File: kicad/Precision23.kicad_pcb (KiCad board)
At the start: 2 copper layers, 76.2 x 76.2 mm, 153 parts, among them J503 STANDOFF, J504 STANDOFF, J505 STANDOFF, J506 STANDOFF, U001 74HC595, U002 74HC595, U101 74HC595, U102 74HC595, U401 ATmega32U4-A, U501 SAM-M8Q, U601 TCR2EF 3.3V, Y401 16MHz

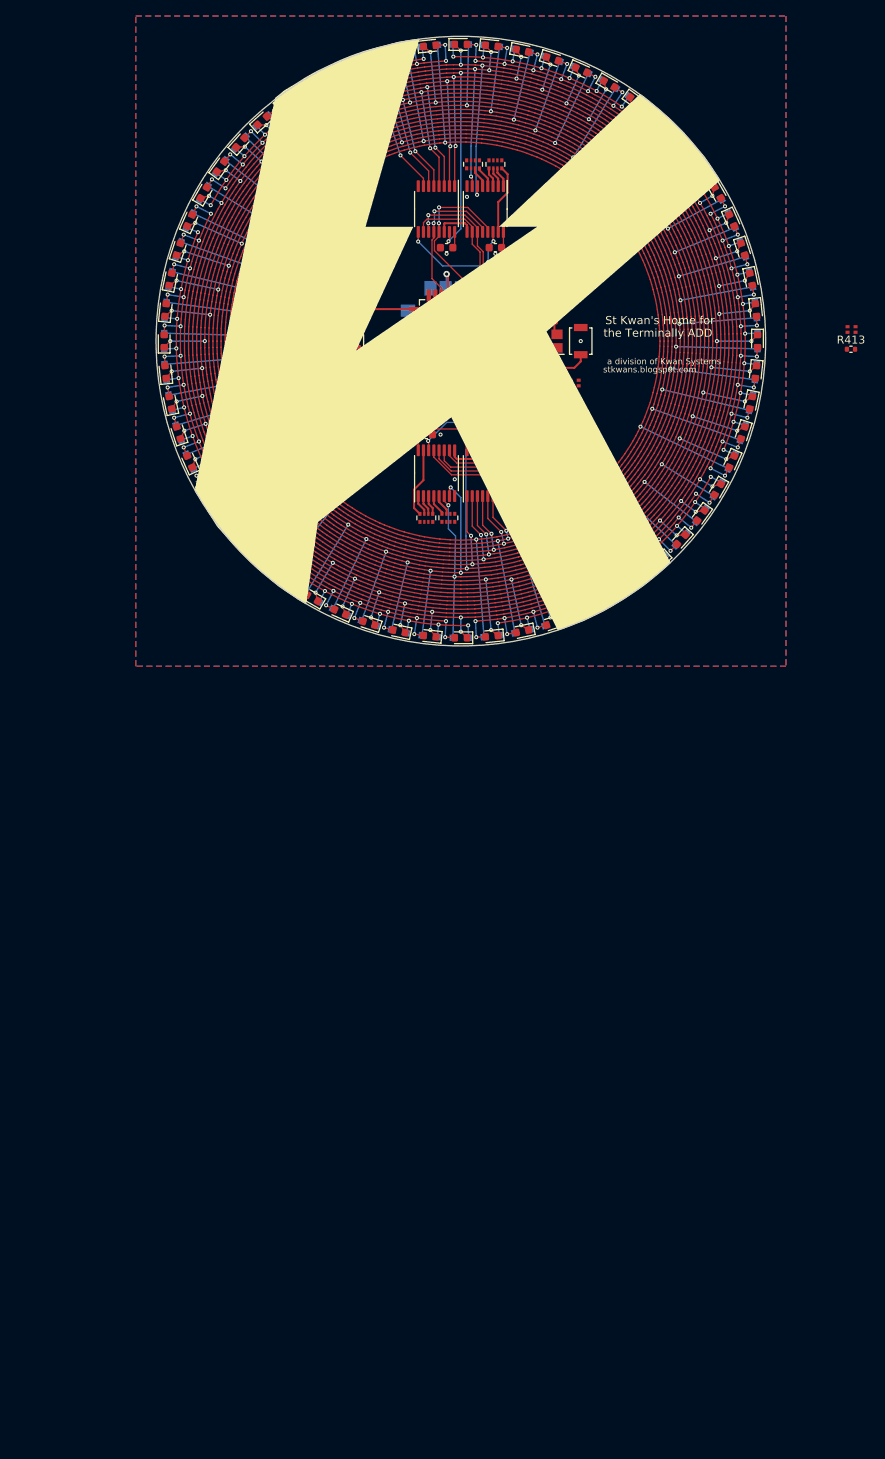
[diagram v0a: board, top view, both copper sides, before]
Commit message: Updated to 3 multiplexers
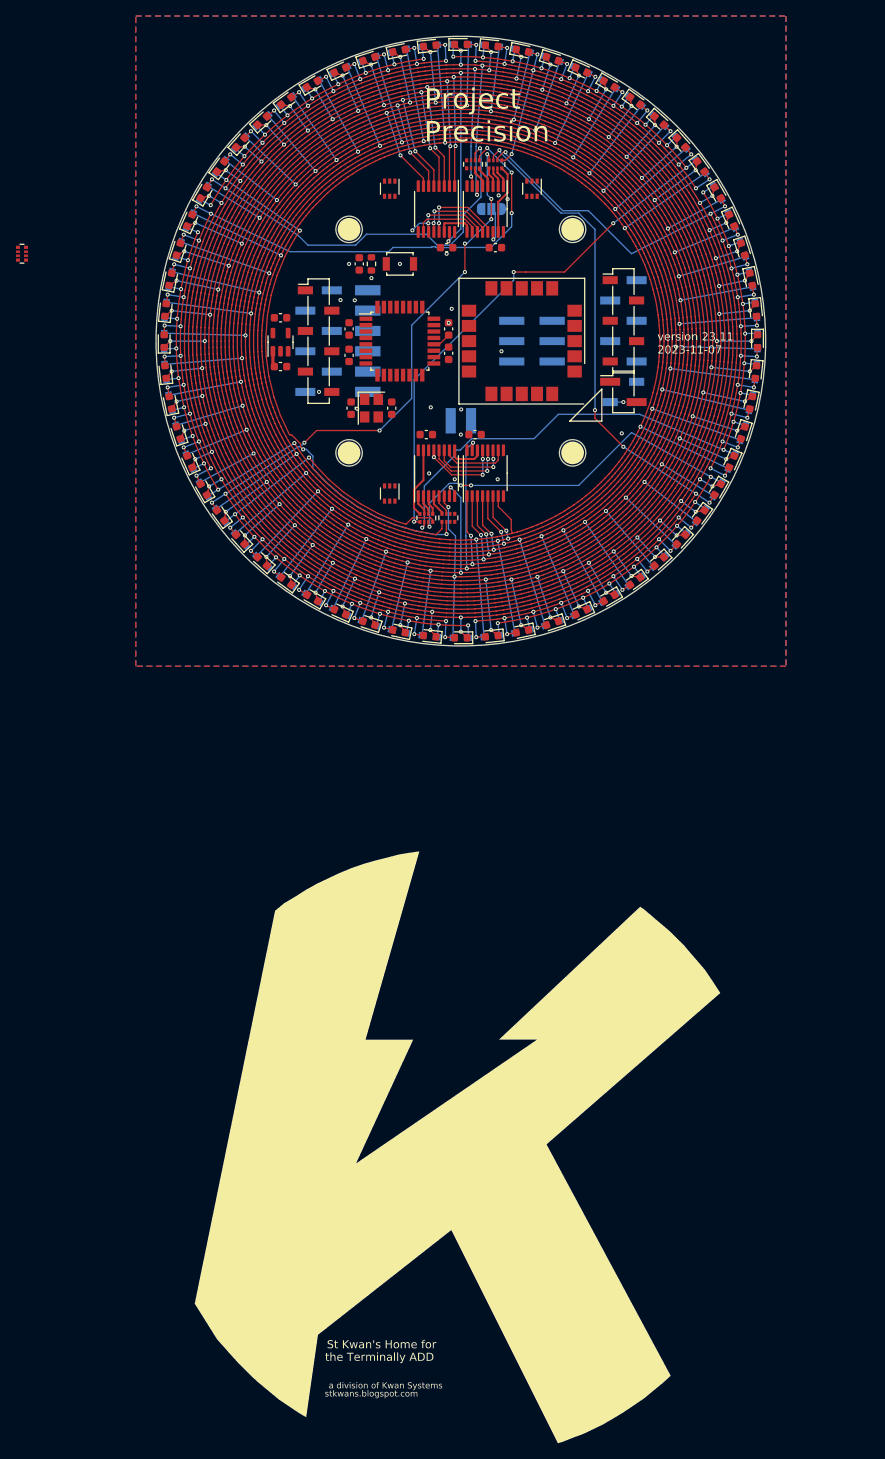
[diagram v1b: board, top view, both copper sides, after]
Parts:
- removed C416, C417: 22pF, Capacitor_SMD:C_0603_1608Metric
- removed C442: 100nF, Capacitor_SMD:C_0603_1608Metric
- removed D401: R, LED_SMD:LED_0603_1608Metric
- removed D402: B, LED_SMD:LED_0603_1608Metric
- removed R403: 22, KwanSystems:R_Array_Convex_2x0402
- removed R408: 330, KwanSystems:R_Array_Convex_2x0402
- removed R413: 10k, Resistor_SMD:R_0402_1005Metric
- removed S413: SW_Push, KwanSystems:SW_SPST_B3U-1000P
- removed Y401: 16MHz, Crystal:Crystal_SMD_3225-4Pin_3.2x2.5mm
- added C404: 100nF, Capacitor_SMD:C_0603_1608Metric, F.Cu at (74.9, 87.4)
- added C407: 22pF, Capacitor_SMD:C_0603_1608Metric, F.Cu at (75.2, 97.3)
- added C408: 22pF, Capacitor_SMD:C_0603_1608Metric, F.Cu at (80.3, 97.3)
- added C418: 100nF, Capacitor_SMD:C_0603_1608Metric, F.Cu at (87.4, 90.4)
- added C420: 100nF, Capacitor_SMD:C_0603_1608Metric, F.Cu at (87.4, 87.4)
- added C506: 100nF, Capacitor_SMD:C_0603_1608Metric, F.Cu at (76.2, 79.2)
- added J501: Conn_01x02_Pin, Connector_PinSocket_2.54mm:PinSocket_1x02_P2.54mm_Vertical_SMD_Pin1Left, B.Cu at (109.2, 95.2)
- added J502: Conn_01x02_Pin, Connector_PinHeader_2.54mm:PinHeader_1x02_P2.54mm_Vertical_SMD_Pin1Left, F.Cu at (109.2, 95.2)
- added J503: Conn_02x03_Odd_Even, Connector_PinHeader_2.54mm:PinHeader_2x03_P2.54mm_Vertical_SMD, B.Cu at (97.8, 88.9)
- added J504: Conn_01x06, KwanSystems:SAMTEC_TSM-106-01-T-SH, B.Cu at (82.5, 88.9)
- added J505: Conn_01x06, Connector_PinHeader_2.54mm:PinHeader_1x06_P2.54mm_Vertical_SMD_Pin1Left, B.Cu at (71.1, 88.9)
- added J506: Conn_01x05, Connector_PinHeader_2.54mm:PinHeader_1x05_P2.54mm_Vertical_SMD_Pin1Left, B.Cu at (109.2, 86.4)
- added J507: Conn_01x05, Connector_PinSocket_2.54mm:PinSocket_1x05_P2.54mm_Vertical_SMD_Pin1Left, F.Cu at (109.2, 86.4)
- added J508: Conn_01x06, Connector_PinSocket_2.54mm:PinSocket_1x06_P2.54mm_Vertical_SMD_Pin1Left, F.Cu at (71.1, 88.9)
- added J509: Conn_01x02_Pin, KwanSystems:SAMTEC_TSM-102-01-T-SH, B.Cu at (88.9, 104.1)
- added R429: 10k, Resistor_SMD:R_0603_1608Metric, F.Cu at (77.7, 79.2)
- added R506: 10k, KwanSystems:R_Array_Convex_4x0402, F.Cu at (34.0, 78.0)
- added S429: SW_SPST, KwanSystems:SW_SPST_B3U-1000P, F.Cu at (81.3, 79.2)
- added S501: SolderJumper_3_Open, Jumper:SolderJumper-3_P1.3mm_Open_RoundedPad1.0x1.5mm, B.Cu at (92.7, 72.4)
- added U502: NC7SZ157, Package_TO_SOT_SMD:SOT-363_SC-70-6, F.Cu at (80.0, 69.8)
- added U503: NC7SZ157, Package_TO_SOT_SMD:SOT-363_SC-70-6, F.Cu at (80.0, 108.0)
- added U504: NC7SZ157, Package_TO_SOT_SMD:SOT-363_SC-70-6, F.Cu at (97.8, 69.8)
- added Y407: 16MHz, Crystal:Crystal_SMD_3225-4Pin_3.2x2.5mm, F.Cu at (77.7, 97.3)
- C406: value 1uF -> 100nF
- U401: value ATmega32U4-A -> ATMEGA328P-AU; footprint Package_QFP:TQFP-44_10x10mm_P0.8mm -> Package_QFP:TQFP-32_7x7mm_P0.8mm
- U501: moved to F.Cu
- moved G101 101.6 mm to (88.9, 190.5)
- moved C406 15.7 mm to (74.9, 90.7), turned to -90 degrees
- moved C601 8.82 mm to (66.4, 92.1)
- moved C605 8.82 mm to (66.4, 86.0)
- moved U601 8.82 mm to (66.4, 89.0)
- moved U401 7.62 mm to (81.3, 88.9), turned to 0 degrees
- moved U501 7.62 mm to (96.5, 88.9), turned to 180 degrees
- renumbered J506 to J596, J505 to J597, J504 to J598, J503 to J599
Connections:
- net /Controller/D12 renamed /Nano/A3
- net /Controller/D8 renamed /Nano/A5
- net /Hour hand/Px0 renamed /Hour hand/Hx0
- net /Hour hand/Px1 renamed /Hour hand/Hx1
- net /Hour hand/Px2 renamed /Hour hand/Hx2
- net /Hour hand/Px3 renamed /Hour hand/Hx3
- net /Hour hand/Px4 renamed /Hour hand/Hx4
- net /Hour hand/Px5 renamed /Hour hand/Hx5
- net /Hour hand/Px6 renamed /Hour hand/Hx6
- net /Hour hand/Px7 renamed /Hour hand/Hx7
- net /Hour hand/Px8 renamed /Hour hand/Hx8
- net /Hour hand/Px9 renamed /Hour hand/Hx9
- net /Hour hand/Q0x renamed /Hour hand/H0x
- net /Hour hand/Q1x renamed /Hour hand/H1x
- net /Hour hand/Q2x renamed /Hour hand/H2x
- net /Hour hand/Q3x renamed /Hour hand/H3x
- net /Hour hand/Q4x renamed /Hour hand/H4x
- net /Hour hand/Q5x renamed /Hour hand/H5x
- net /Hour hand/SEROUT renamed /SER_HR_MN
- net /Minute hand/Px0 renamed /Minute hand/Mx0
- net /Minute hand/Px1 renamed /Minute hand/Mx1
- net /Minute hand/Px2 renamed /Minute hand/Mx2
- net /Minute hand/Px3 renamed /Minute hand/Mx3
- net /Minute hand/Px4 renamed /Minute hand/Mx4
- net /Minute hand/Px5 renamed /Minute hand/Mx5
- net /Minute hand/Px6 renamed /Minute hand/Mx6
- net /Minute hand/Px7 renamed /Minute hand/Mx7
- net /Minute hand/Px8 renamed /Minute hand/Mx8
- net /Minute hand/Px9 renamed /Minute hand/Mx9
- net /Minute hand/Q0x renamed /Minute hand/M0x
- net /Minute hand/Q1x renamed /Minute hand/M1x
- net /Minute hand/Q2x renamed /Minute hand/M2x
- net /Minute hand/Q3x renamed /Minute hand/M3x
- net /Minute hand/Q4x renamed /Minute hand/M4x
- net /Minute hand/Q5x renamed /Minute hand/M5x
- C406 pad 1: GND -> +3V3
- C406 pad 2: /Controller/UCAP -> GND
- U001 pad 10: /Controller/D4 -> /Nano/D4
- U001 pad 11: /Controller/D3 -> /Nano/D3
- U001 pad 12: /Controller/D5 -> /Nano/D5
- U001 pad 13: /Controller/D6 -> /Nano/D6
- U001 pad 14: /Controller/D2 -> /SER_IN
- U002 pad 10: /Controller/D4 -> /Nano/D4
- U002 pad 11: /Controller/D3 -> /Nano/D3
- U002 pad 12: /Controller/D5 -> /Nano/D5
- U002 pad 13: /Controller/D6 -> /Nano/D6
- U101 pad 10: /Controller/D4 -> /Nano/D4
- U101 pad 11: /Controller/D3 -> /Nano/D3
- U101 pad 12: /Controller/D5 -> /Nano/D5
- U101 pad 13: /Controller/D6 -> /Nano/D6
- U102 pad 10: /Controller/D4 -> /Nano/D4
- U102 pad 11: /Controller/D3 -> /Nano/D3
- U102 pad 12: /Controller/D5 -> /Nano/D5
- U102 pad 13: /Controller/D6 -> /Nano/D6
- U102 pad 9: /Minute hand/SEROUT -> /SER_MN_SC
- U401 pad 1: /Controller/D7 -> /Nano/D3
- U401 pad 10: /Controller/D16 -> /Nano/D6
- U401 pad 11: /Controller/D14 -> /Nano/D7
- U401 pad 12: /Controller/D11 -> /Nano/D8
- U401 pad 13: Net-(U401-~{RESET}) -> /Nano/D9
- U401 pad 14: +3V3 -> /Nano/D10
- U401 pad 15: GND -> /Nano/D11
- U401 pad 16: /Controller/XTAL2 -> /Nano/D12
- U401 pad 17: /Controller/XTAL1 -> /Nano/D13
- U401 pad 18: /Controller/D3 -> +3V3
- U401 pad 19: /Controller/D2 -> /Nano/A6
- U401 pad 2: VBUS -> /Nano/D4
- U401 pad 20: /GPS_TX -> /Nano/AREF
- U401 pad 21: /GPS_RX -> GND
- U401 pad 22: /Controller/TXLED -> /Nano/A7
- U401 pad 23: GND -> /Nano/A0
- U401 pad 24: +3V3 -> /Nano/A1
- U401 pad 25: /Controller/D4 -> /Nano/A2
- U401 pad 27: /Controller/D6 -> /Nano/A4
- U401 pad 29: /Controller/D9 -> /~{RESET}
- U401 pad 3: /Controller/Q_D- -> GND
- U401 pad 30: /Controller/D10 -> /AT_RX
- U401 pad 31: /Controller/D5 -> /AT_TX
- U401 pad 32: /Controller/D13 -> /Nano/D2
- U401 pad 4: /Controller/Q_D+ -> +3V3
- U401 pad 6: /Controller/UCAP -> +3V3
- U401 pad 7: VBUS -> /Nano/XTAL1
- U401 pad 8: /Controller/D17 -> /Nano/XTAL2
- U401 pad 9: /Controller/D15 -> /Nano/D5
- U501 pad 7: /Controller/D10 -> /Nano/D10
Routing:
- net +3V3: track 78.6 -> 0.00 mm, vias 1 -> 0
- net /Minute hand/M5x: track 48.8 -> 113.4 mm, vias 10 -> 13
- net /Minute hand/M0x: track 48.7 -> 112.3 mm, vias 10 -> 13
- net /Hour hand/H3x: track 63.1 -> 126.4 mm, vias 20 -> 27
- net /Hour hand/H2x: track 63.1 -> 120.3 mm, vias 20 -> 23
- net /Hour hand/H4x: track 63.0 -> 116.1 mm, vias 20 -> 23
- net /SER_HR_MN: track 49.3 -> 0.00 mm, vias 2 -> 0
- net /Minute hand/M1x: track 48.7 -> 97.2 mm, vias 10 -> 11
- net /Hour hand/H5x: track 63.1 -> 110.1 mm, vias 20 -> 21
- net /Minute hand/M2x: track 48.8 -> 92.8 mm, vias 10 -> 13
- net /Controller/D3: track 35.9 -> 0.00 mm, vias 4 -> 0
- net /Minute hand/M4x: track 48.7 -> 83.6 mm, vias 10 -> 11
- net /Hour hand/H1x: track 63.0 -> 96.8 mm, vias 20 -> 21
- net /Controller/D6: track 31.6 -> 0.00 mm, vias 4 -> 0
- net /Minute hand/M3x: track 48.8 -> 79.4 mm, vias 10 -> 11
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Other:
- board text added: "HR MN"
- board text added: "Hand Select"
- board text added: "Project Precision"
- board text added: "SC TH"
- board text added: "version 23.11 2023-11-07"
